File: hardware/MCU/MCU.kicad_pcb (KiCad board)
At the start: 2 copper layers, 40 x 40 mm, 41 parts, among them P1 CONN_01X05, P2 CONN_01X04, P3 CONN_01X05, P4 CONN_01X05, U1 MAX6369, U2 TC1262-30VDB, U3 DS18B20, U4 PIC18F45K22, U5 LT6005, Y1 Crystal

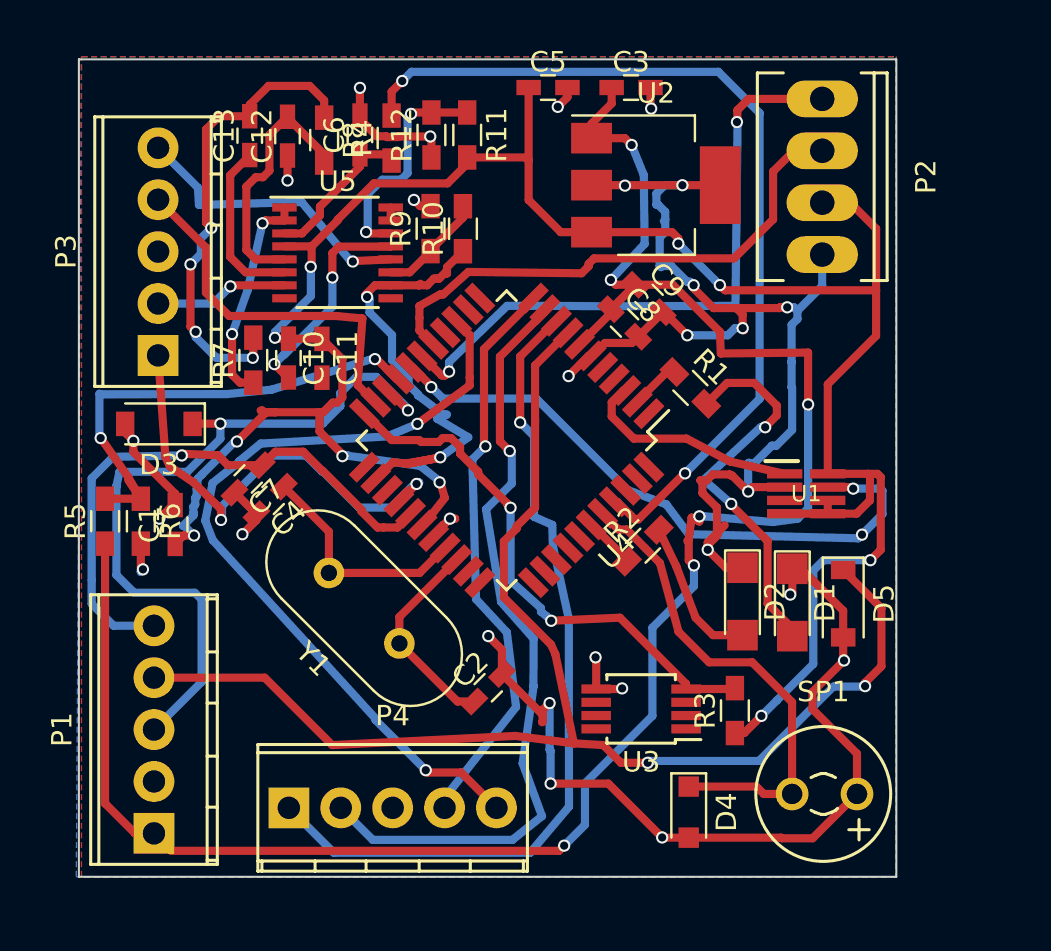
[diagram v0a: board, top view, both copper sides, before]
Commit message: MCU: Añadidos ficheros de fabricacion. Lista para fabricar la versión 1.0 a falta de retoques de serigrafía (logo)
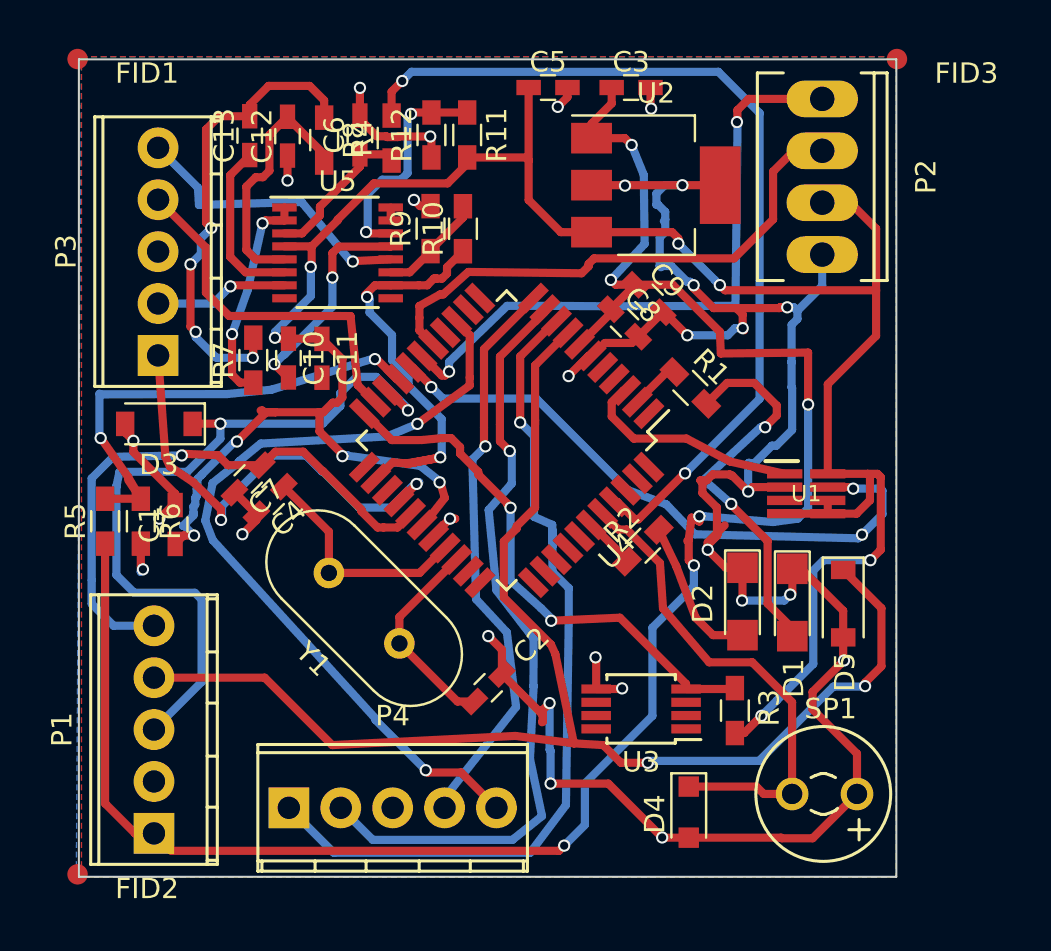
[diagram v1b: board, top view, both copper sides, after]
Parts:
- added FID1: FIDUCIAL, Fiducials:Fiducial_1mm_Dia_2.54mm_Outer_CopperTop, F.Cu at (12.0, 158.1)
- added FID2: FIDUCIAL, Fiducials:Fiducial_1mm_Dia_2.54mm_Outer_CopperTop, F.Cu at (12.0, 198.0)
- added FID3: FIDUCIAL, Fiducials:Fiducial_1mm_Dia_2.54mm_Outer_CopperTop, F.Cu at (52.1, 158.1)
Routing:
- net GND: track 135.8 -> 139.9 mm, vias 30 -> 31
- net /F_RF_IN: track 24.4 -> 22.2 mm
- net /PTT: track 41.1 -> 42.1 mm
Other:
- board text added: "D1"
- board text added: "D2"
- board text added: "D4"
- board text added: "D5"
- board text added: "P1"
- board text added: "P2"
- board text added: "P3"
- board text added: "P4"
- board text added: "U3"
